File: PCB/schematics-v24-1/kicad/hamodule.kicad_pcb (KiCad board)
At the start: 4 copper layers, 129.6 x 83.3 mm, 188 parts, among them J1 GND|5V, J10 Tx|Rx, J11 Sda|Scl, J12 3|9, J13 13|12, J14 3.3v|GND|7|15, J15 2604-1104, J16 2604-1104, J17 TestPoint, J19 TestPoint, J2 2604-1102, J3 USB_C_Receptacle_USB2.0, J4 GND|3.3V, J5 Conn_01x02_Pin, J6 2604-1104, J7 2604-1104, J8 5v|GND|Do, J9 Screen, K1 AQG22205, K2 AQG22205, K3 AQG22205, K4 AQG22205, K5 AQG22205, K6 AQG22205, K7 AQG22205, K8 AQG22205, SW1 USB | PS, SW2 Reset, SW3 Boot, U1 LD1117AV33, U10 SN74LV1T34DBV, U11 ULN2803A, U12 TCAL6416, U2 USBLC6-2SC6, U3 ESP32-S3-WROOM-2, U4 LDA210-PDIP, U5 LDA210-PDIP, U6 LDA210-PDIP, U7 LDA210-PDIP, U8 SHT4x, U9 TXB0108PW

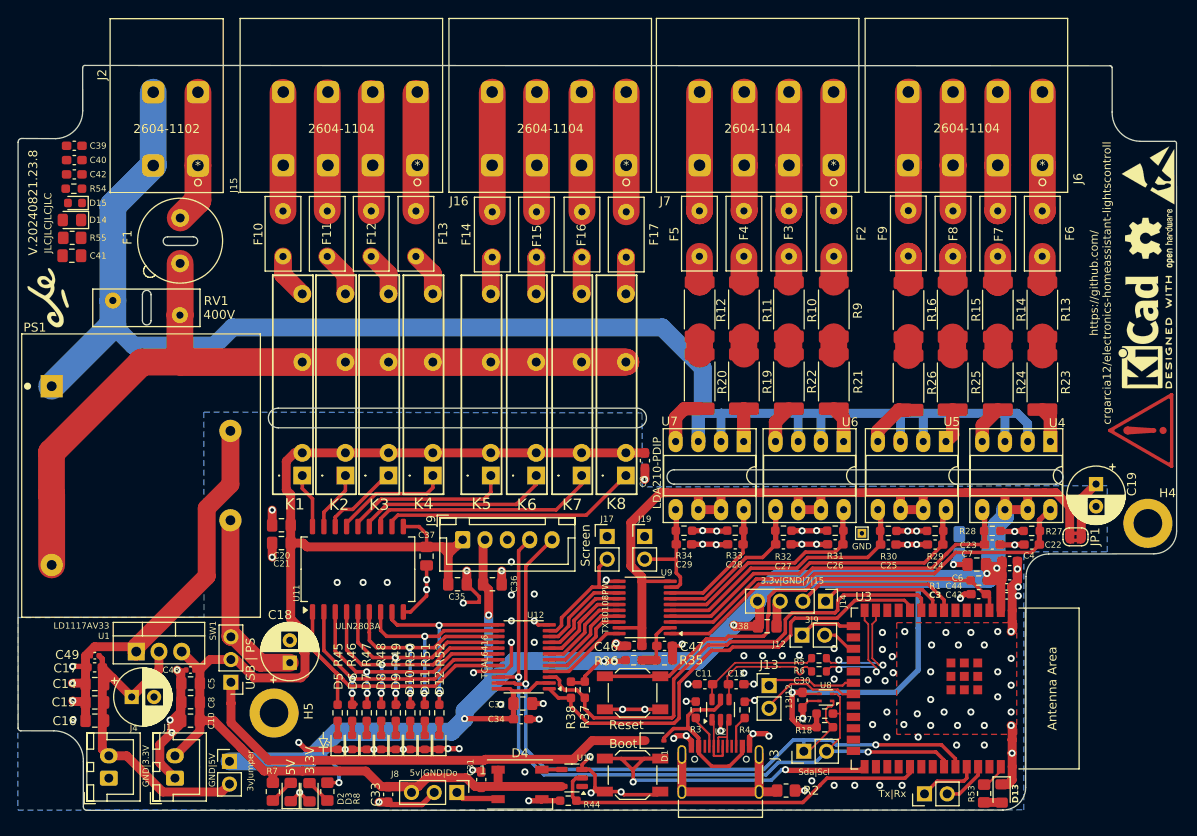
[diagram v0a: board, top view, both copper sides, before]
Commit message: adding pull down resistors between I2C and ULN
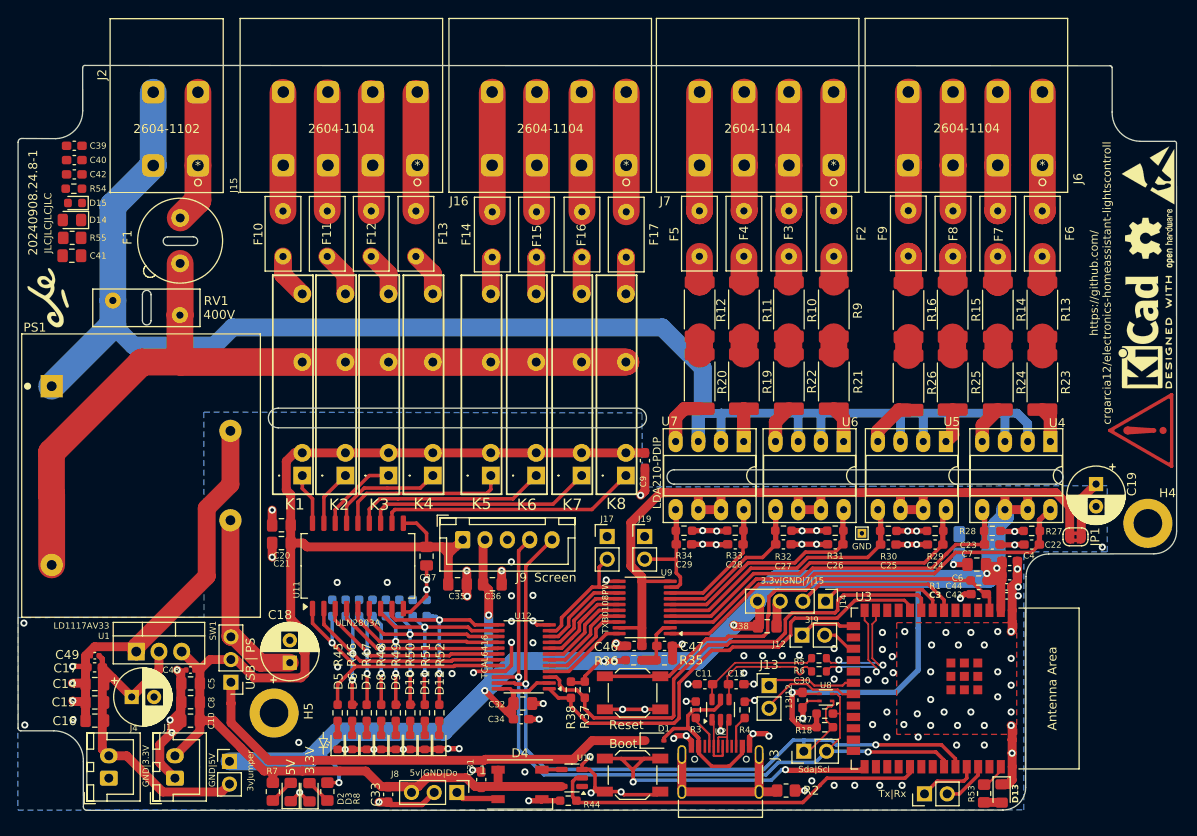
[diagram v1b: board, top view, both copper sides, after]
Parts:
- added R39: 10kΩ, Resistor_SMD:R_0603_1608Metric_Pad0.98x0.95mm_HandSolder, B.Cu at (59.0, 92.9)
- added R40: 10kΩ, Resistor_SMD:R_0603_1608Metric_Pad0.98x0.95mm_HandSolder, B.Cu at (60.5, 92.9)
- added R41: 10kΩ, Resistor_SMD:R_0603_1608Metric_Pad0.98x0.95mm_HandSolder, B.Cu at (62.0, 92.9)
- added R42: 10kΩ, Resistor_SMD:R_0603_1608Metric_Pad0.98x0.95mm_HandSolder, B.Cu at (63.5, 92.9)
- added R43: 10kΩ, Resistor_SMD:R_0603_1608Metric_Pad0.98x0.95mm_HandSolder, B.Cu at (65.0, 92.9)
- added R56: 10kΩ, Resistor_SMD:R_0603_1608Metric_Pad0.98x0.95mm_HandSolder, B.Cu at (66.5, 92.9)
- added R57: 10kΩ, Resistor_SMD:R_0603_1608Metric_Pad0.98x0.95mm_HandSolder, B.Cu at (68.0, 92.9)
- added R58: 10kΩ, Resistor_SMD:R_0603_1608Metric_Pad0.98x0.95mm_HandSolder, B.Cu at (69.6, 92.9)
- moved U11 0.38 mm to (61.9, 88.2)
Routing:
- net Net-(U11-I6): track 35.3 -> 26.5 mm
- net GND: track 229.5 -> 223.9 mm, vias 126 -> 129
- net Net-(U11-I1): track 36.7 -> 32.6 mm, vias 0 -> 1
- net 3.3V+: track 327.7 -> 331.7 mm
- net Net-(U11-I2): track 29.0 -> 33.0 mm
- net Net-(U11-I3): track 28.0 -> 31.1 mm
- net Net-(U11-I8): track 21.9 -> 24.3 mm
- net Net-(U11-I4): track 27.2 -> 29.5 mm
- net Net-(U11-I5): track 25.8 -> 28.0 mm
- net Net-(U11-I7): track 23.4 -> 24.9 mm
- net Net-(U11-O5): track 18.6 -> 19.4 mm
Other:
- board text added: "20240908.24.8-1"
- board text removed: "V.20240821.23.8"
